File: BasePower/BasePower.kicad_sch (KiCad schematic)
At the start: 9 parts, among them J1 VIN, J2 3.3V

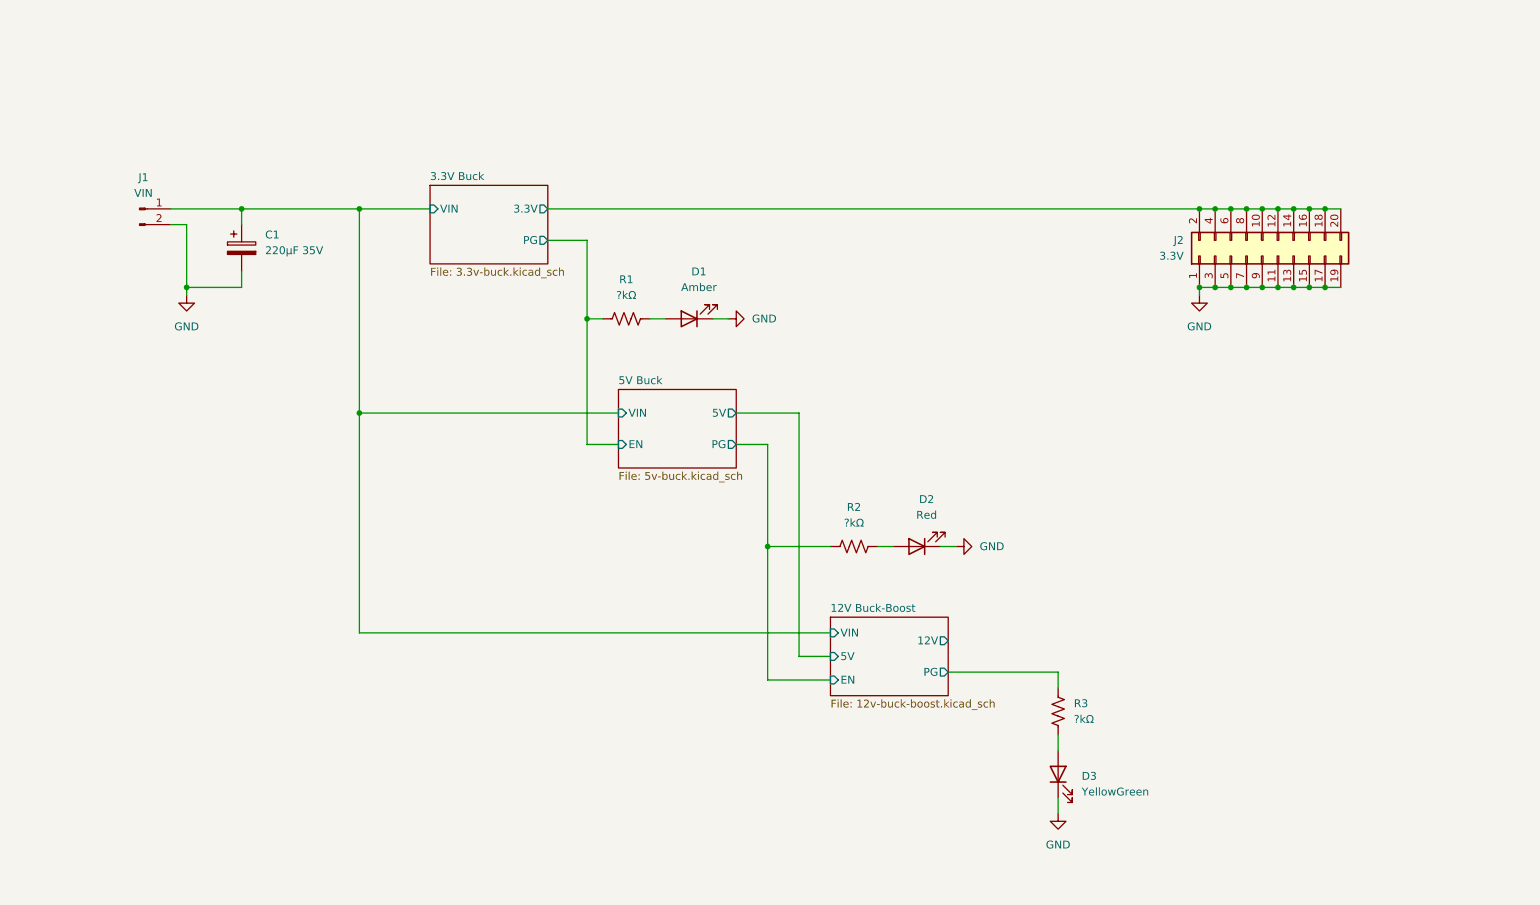
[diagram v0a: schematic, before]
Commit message: BasePower layout mostly done
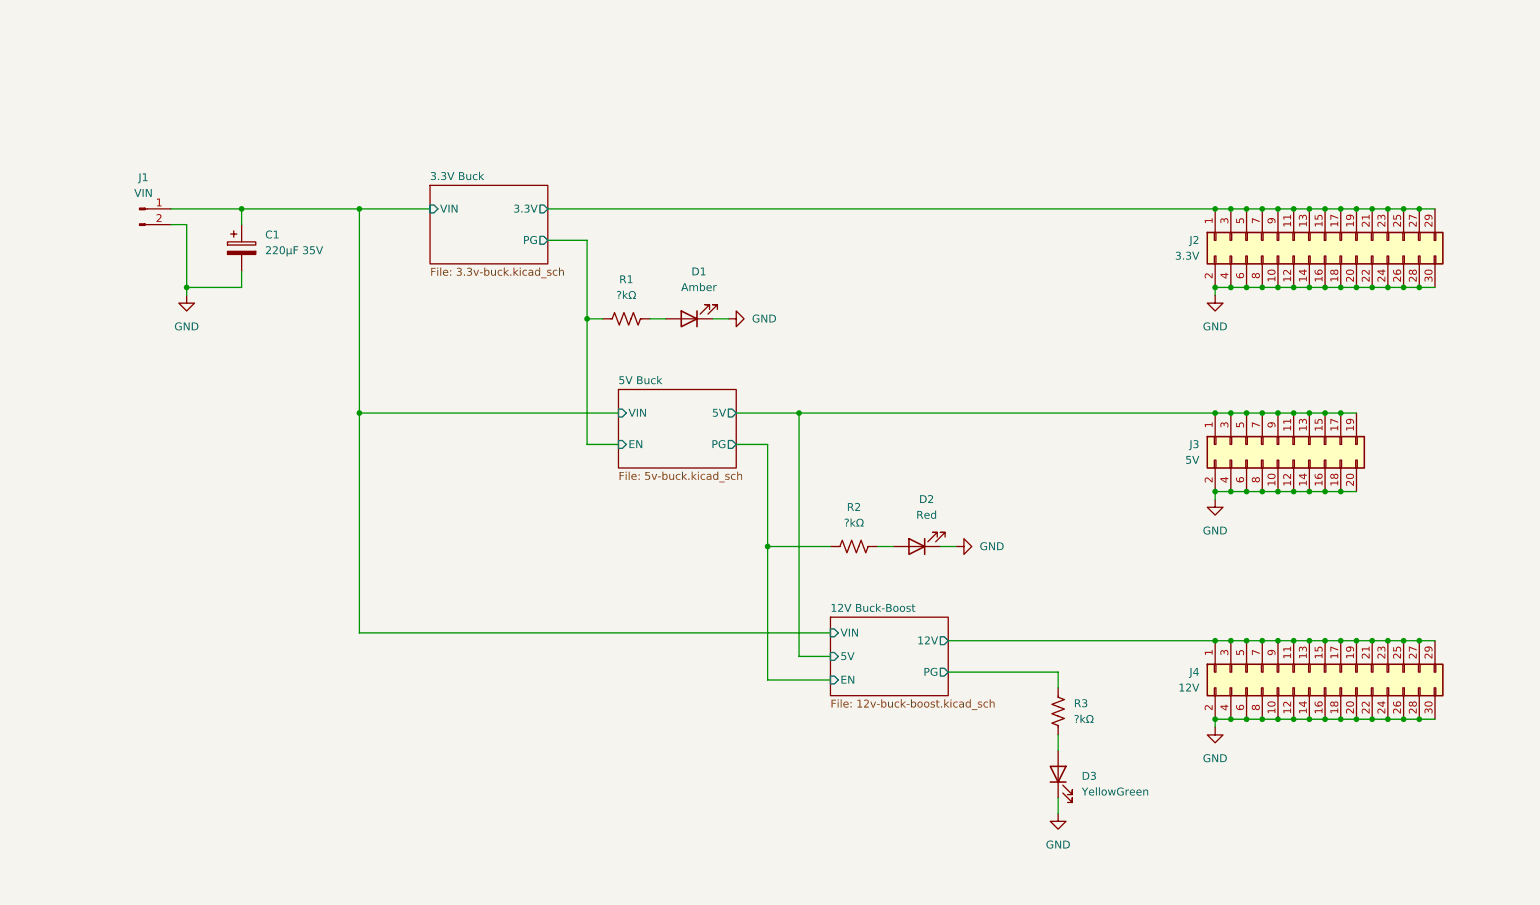
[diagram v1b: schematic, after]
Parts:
- removed J2: 3.3V, Connector_PinHeader_2.54mm:PinHeader_2x10_P2.54mm_Vertical, symbol Connector_Generic:Conn_02x10_Odd_Even
- added J2: 3.3V, Connector_PinHeader_2.54mm:PinHeader_2x15_P2.54mm_Vertical, symbol Connector_Generic:Conn_02x15_Odd_Even
- added J3: 5V, Connector_PinHeader_2.54mm:PinHeader_2x10_P2.54mm_Vertical, symbol Connector_Generic:Conn_02x10_Odd_Even
- added J4: 12V, Connector_PinHeader_2.54mm:PinHeader_2x15_P2.54mm_Vertical, symbol Connector_Generic:Conn_02x15_Odd_Even
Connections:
- net 12V Buck-Boost/12V: now also J4.1 (Pin_1), J4.11 (Pin_11), J4.13 (Pin_13), J4.15 (Pin_15), J4.17 (Pin_17), J4.19 (Pin_19), J4.21 (Pin_21), J4.23 (Pin_23), J4.25 (Pin_25), J4.27 (Pin_27), J4.29 (Pin_29), J4.3 (Pin_3), J4.5 (Pin_5), J4.7 (Pin_7), J4.9 (Pin_9)
- net 12V Buck-Boost/5V: now also J3.1 (Pin_1), J3.11 (Pin_11), J3.13 (Pin_13), J3.15 (Pin_15), J3.17 (Pin_17), J3.19 (Pin_19), J3.3 (Pin_3), J3.5 (Pin_5), J3.7 (Pin_7), J3.9 (Pin_9)
- net 3.3V Buck/3.3V: now also J2.1 (Pin_1), J2.11 (Pin_11), J2.13 (Pin_13), J2.15 (Pin_15), J2.17 (Pin_17), J2.19 (Pin_19), J2.21 (Pin_21), J2.23 (Pin_23), J2.25 (Pin_25), J2.27 (Pin_27), J2.29 (Pin_29), J2.3 (Pin_3), J2.5 (Pin_5), J2.7 (Pin_7), J2.9 (Pin_9)
- net GND: now also J2.10 (Pin_10), J2.12 (Pin_12), J2.14 (Pin_14), J2.16 (Pin_16), J2.18 (Pin_18), J2.2 (Pin_2), J2.20 (Pin_20), J2.22 (Pin_22), J2.24 (Pin_24), J2.26 (Pin_26), J2.28 (Pin_28), J2.30 (Pin_30), J2.4 (Pin_4), J2.6 (Pin_6), J2.8 (Pin_8), J3.10 (Pin_10), J3.12 (Pin_12), J3.14 (Pin_14), J3.16 (Pin_16), J3.18 (Pin_18), J3.2 (Pin_2), J3.20 (Pin_20), J3.4 (Pin_4), J3.6 (Pin_6), J3.8 (Pin_8), J4.10 (Pin_10), J4.12 (Pin_12), J4.14 (Pin_14), J4.16 (Pin_16), J4.18 (Pin_18), J4.2 (Pin_2), J4.20 (Pin_20), J4.22 (Pin_22), J4.24 (Pin_24), J4.26 (Pin_26), J4.28 (Pin_28), J4.30 (Pin_30), J4.4 (Pin_4), J4.6 (Pin_6), J4.8 (Pin_8)

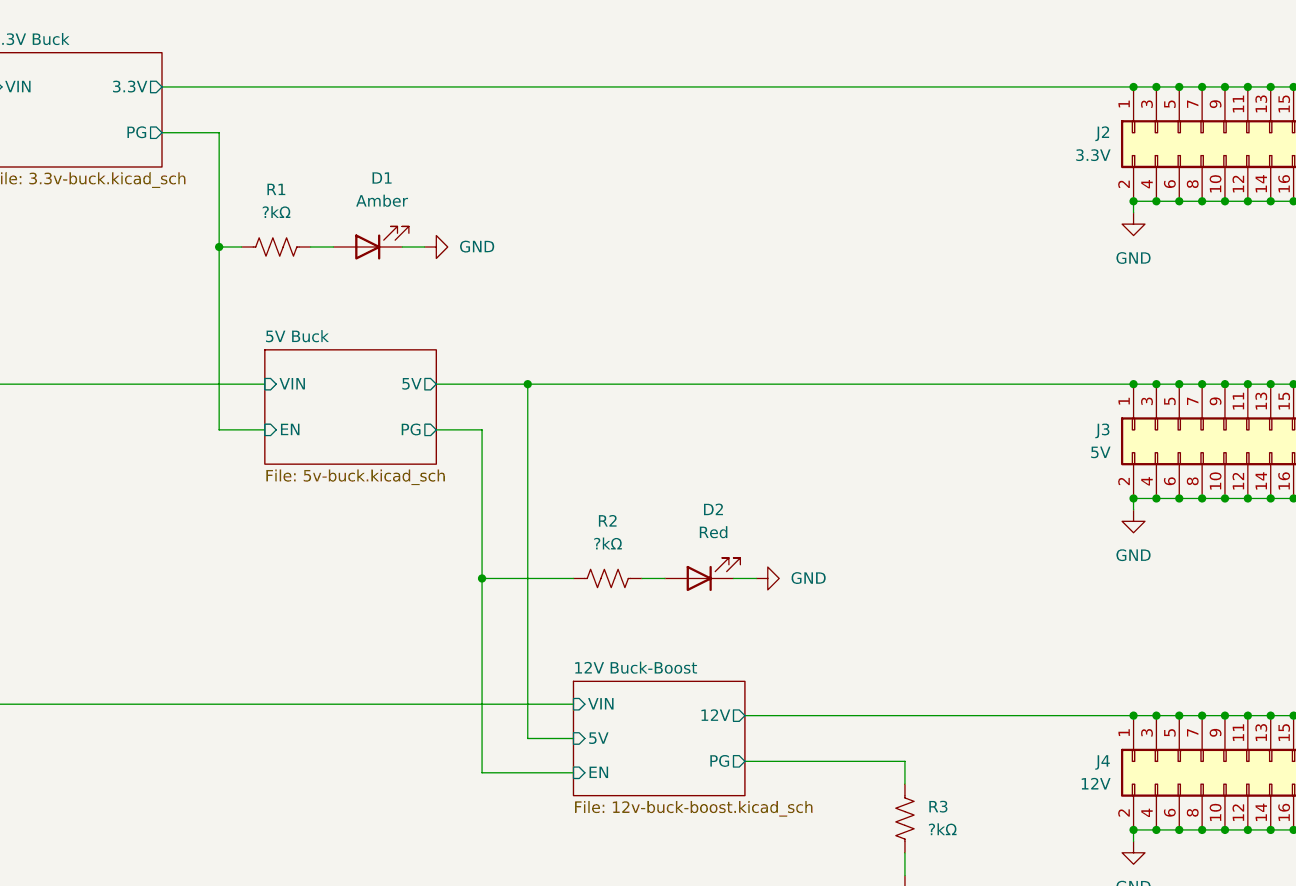
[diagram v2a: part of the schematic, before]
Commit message: BasePower v1.1: Now with fuses
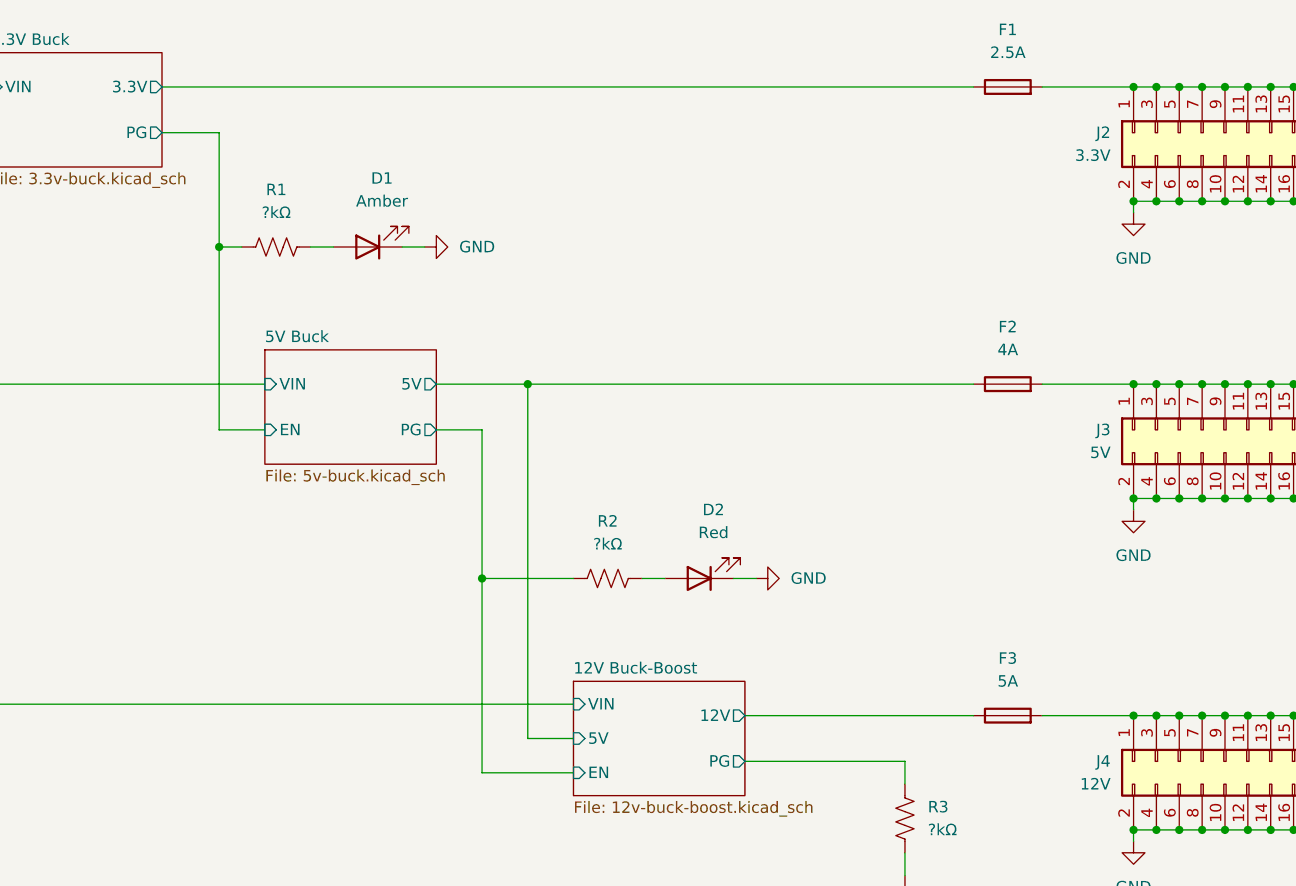
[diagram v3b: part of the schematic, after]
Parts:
- added F1: 2.5A, Fuse:Fuse_0603_1608Metric, symbol Device:Fuse
- added F2: 4A, Fuse:Fuse_0603_1608Metric, symbol Device:Fuse
- added F3: 5A, Fuse:Fuse_0603_1608Metric, symbol Device:Fuse
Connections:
- net 12V Buck-Boost/12V: now also F3.1; no longer J4.1 (Pin_1), J4.11 (Pin_11), J4.13 (Pin_13), J4.15 (Pin_15), J4.17 (Pin_17), J4.19 (Pin_19), J4.21 (Pin_21), J4.23 (Pin_23), J4.25 (Pin_25), J4.27 (Pin_27), J4.29 (Pin_29), J4.3 (Pin_3), J4.5 (Pin_5), J4.7 (Pin_7), J4.9 (Pin_9)
- net 12V Buck-Boost/5V: now also F2.1; no longer J3.1 (Pin_1), J3.11 (Pin_11), J3.13 (Pin_13), J3.15 (Pin_15), J3.17 (Pin_17), J3.19 (Pin_19), J3.3 (Pin_3), J3.5 (Pin_5), J3.7 (Pin_7), J3.9 (Pin_9)
- net 3.3V Buck/3.3V: now also F1.1; no longer J2.1 (Pin_1), J2.11 (Pin_11), J2.13 (Pin_13), J2.15 (Pin_15), J2.17 (Pin_17), J2.19 (Pin_19), J2.21 (Pin_21), J2.23 (Pin_23), J2.25 (Pin_25), J2.27 (Pin_27), J2.29 (Pin_29), J2.3 (Pin_3), J2.5 (Pin_5), J2.7 (Pin_7), J2.9 (Pin_9)
- new net: F2.2, J3.1 (Pin_1), J3.11 (Pin_11), J3.13 (Pin_13), J3.15 (Pin_15), J3.17 (Pin_17), J3.19 (Pin_19), J3.3 (Pin_3), J3.5 (Pin_5), J3.7 (Pin_7), J3.9 (Pin_9)
- new net: F3.2, J4.1 (Pin_1), J4.11 (Pin_11), J4.13 (Pin_13), J4.15 (Pin_15), J4.17 (Pin_17), J4.19 (Pin_19), J4.21 (Pin_21), J4.23 (Pin_23), J4.25 (Pin_25), J4.27 (Pin_27), J4.29 (Pin_29), J4.3 (Pin_3), J4.5 (Pin_5), J4.7 (Pin_7), J4.9 (Pin_9)
- new net: F1.2, J2.1 (Pin_1), J2.11 (Pin_11), J2.13 (Pin_13), J2.15 (Pin_15), J2.17 (Pin_17), J2.19 (Pin_19), J2.21 (Pin_21), J2.23 (Pin_23), J2.25 (Pin_25), J2.27 (Pin_27), J2.29 (Pin_29), J2.3 (Pin_3), J2.5 (Pin_5), J2.7 (Pin_7), J2.9 (Pin_9)

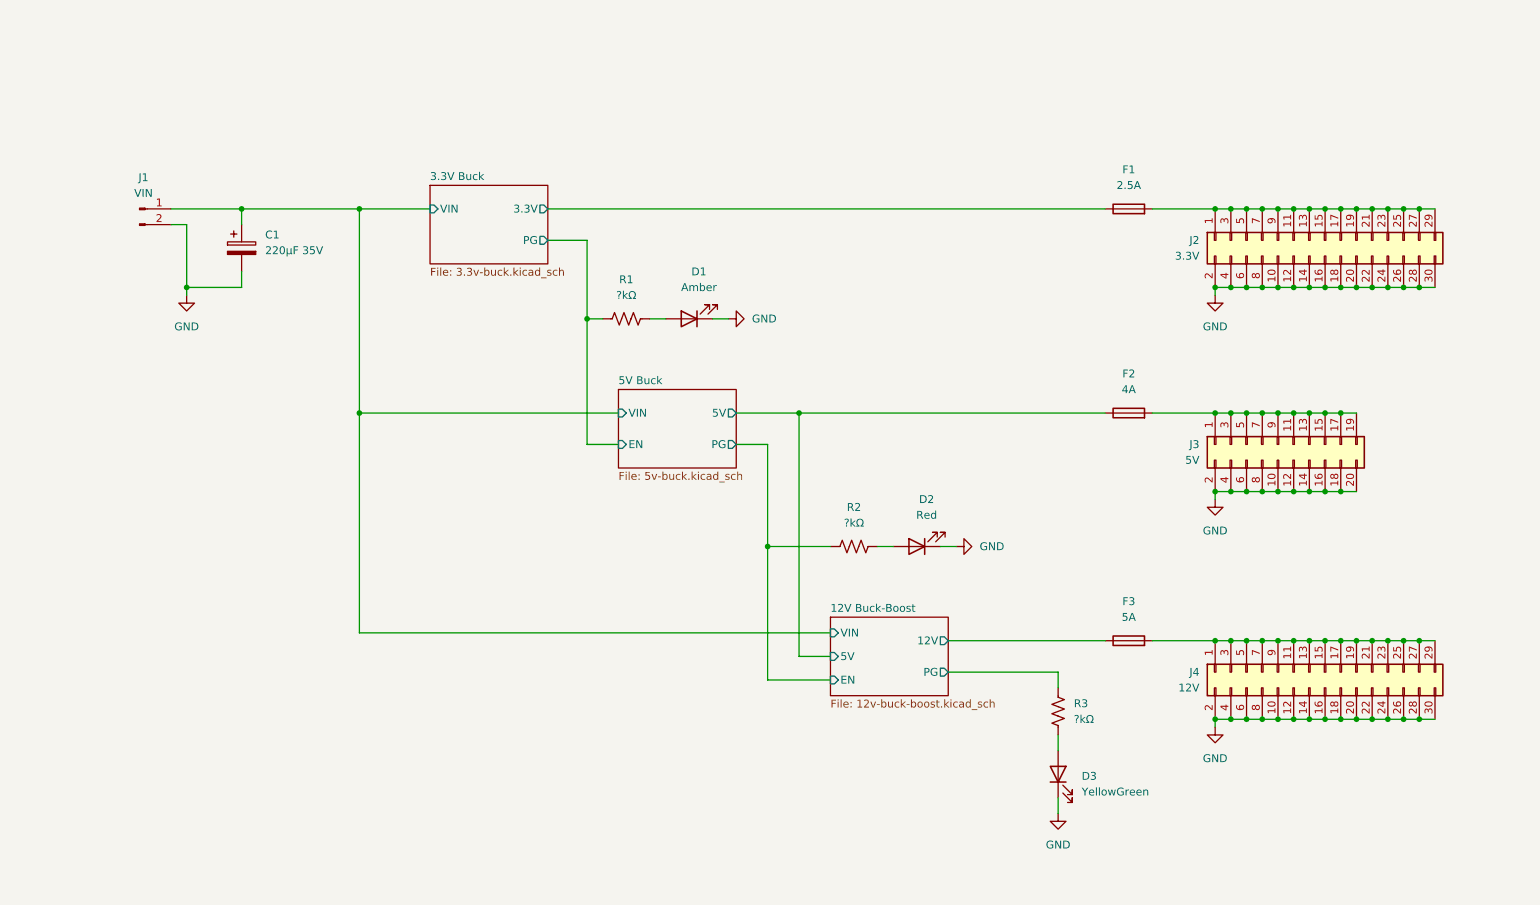
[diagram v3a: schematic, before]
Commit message: BasePower v1.2 + inventory
Added 12V clean LDO and improved power good display
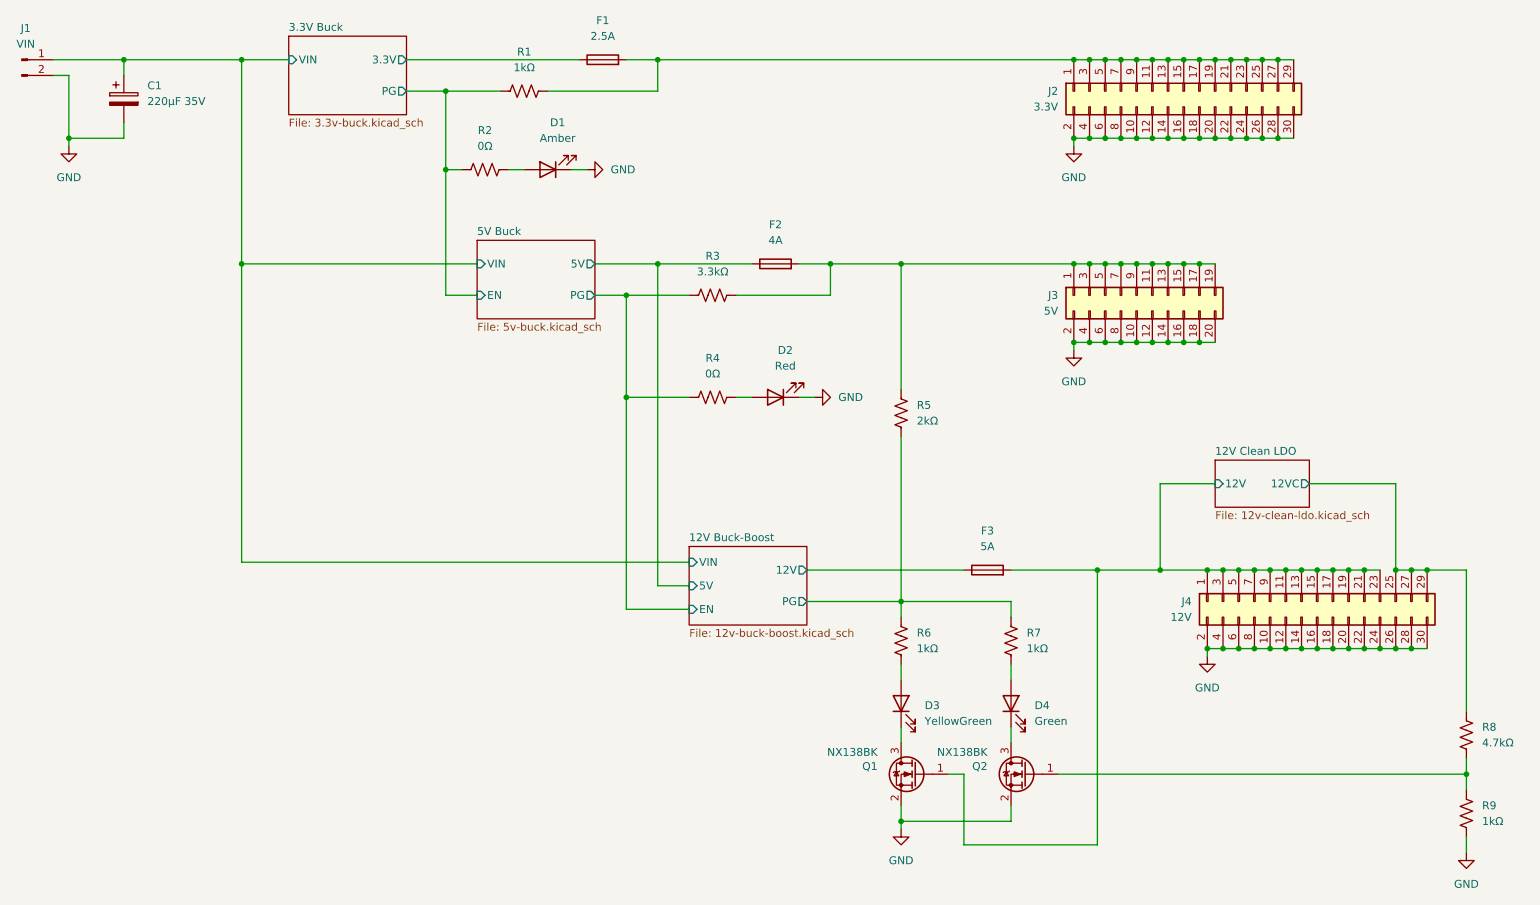
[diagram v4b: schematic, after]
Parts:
- added D4: Green, LED_SMD:LED_0603_1608Metric, symbol Device:LED
- added Q1, Q2: NX138BK, Package_TO_SOT_SMD:SOT-23, symbol Device:Q_NMOS_GSD
- added R1, R7, R9: 1kΩ, Resistor_SMD:R_0603_1608Metric, symbol Device:R_US
- added R3: 3.3kΩ, Resistor_SMD:R_0603_1608Metric, symbol Device:R_US
- added R5: 2kΩ, Resistor_SMD:R_0603_1608Metric, symbol Device:R_US
- added R8: 4.7kΩ, Resistor_SMD:R_0603_1608Metric, symbol Device:R_US
- R2: renamed from R1; value ?kΩ -> 0Ω
- R4: renamed from R2; value ?kΩ -> 0Ω
- R6: renamed from R3; value ?kΩ -> 1kΩ
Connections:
- net 12V Buck-Boost/EN: now also R3.1
- net 12V Buck-Boost/PG: now also R5.1, R7.1
- net 3.3V Buck/PG: now also R1.1
- net GND: now also Q1.2 (S), Q2.2 (S), R9.2; no longer D3.1 (K)
- net at F2.2, J3.1 (Pin_1), J3.11 (Pin_11)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: now also R3.2, R5.2
- net 12V Clean LDO/12V: now reaches F3.2, J4.1 (Pin_1), J4.11 (Pin_11), J4.13 (Pin_13), J4.15 (Pin_15), J4.17 (Pin_17), J4.19 (Pin_19), J4.21 (Pin_21), J4.23 (Pin_23), J4.3 (Pin_3), J4.5 (Pin_5), J4.7 (Pin_7), J4.9 (Pin_9)
- net 12V Clean LDO/12V: now also Q1.1 (G); no longer J4.25 (Pin_25), J4.27 (Pin_27), J4.29 (Pin_29)
- net at F1.2, J2.1 (Pin_1), J2.11 (Pin_11)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: now also R1.2
- new net: Q2.1 (G), R8.2, R9.1
- new net: D4.1 (K), Q2.3 (D)
- new net: D3.1 (K), Q1.3 (D)
- new net: D4.2 (A), R7.2
- new net 12V Clean LDO/12VC: J4.25 (Pin_25), J4.27 (Pin_27), J4.29 (Pin_29), R8.1
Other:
- added sheet 12V Clean LDO (12v-clean-ldo.kicad_sch)
- moved on the sheet: C1, D1, D2, D3, F1, F2, F3, J1, J2, J3, J4, R2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

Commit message: BasePower adjusted LED resistors for equal brightness
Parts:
- R6: value 1kΩ -> 510Ω
- R7: value 1kΩ -> 2.2kΩ
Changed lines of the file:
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@@
 			)
 		)
-		(property "Value" "1kΩ"
+		(property "Value" "510Ω"
 			(at 166.37 120.6499 0)
 			(effects
@@
 			)
 		)
-		(property "Value" "1kΩ"
+		(property "Value" "2.2kΩ"
 			(at 184.15 120.6499 0)
 			(effects
